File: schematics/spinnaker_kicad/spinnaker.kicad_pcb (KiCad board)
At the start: 2 copper layers, 87 x 60.3 mm, 156 parts, among them J1 L_INP, J2 R_INP, J3 L_OUT, J4 R_OUT, J5 9VDC POWER, J6 CONTROL, Q1 AO3401, U1 SpinSemi_FV-1, U10 24LC32, U11 24LC32, U12 24LC32, U13 24LC32, U14 24LC32, U15 24LC32, U16 24LC32, U17 AMS1117-3.3, U18 AMS1117-5.0, U19 MP1470, U2 TL071, U3 TL071, U4 TL071, U5 TL071, U6 PT2258, U7 MCP4728, U8 PCF8574, U9 24LC32, Y1 32768Hz

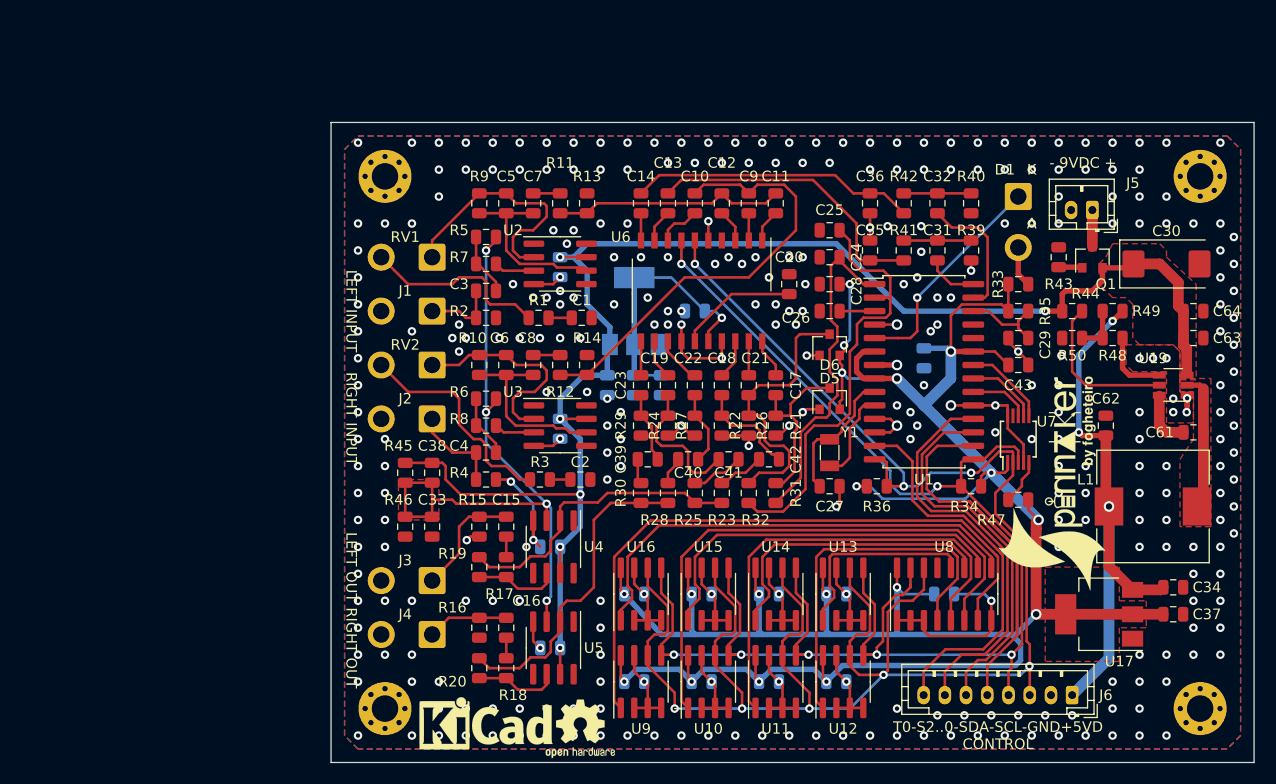
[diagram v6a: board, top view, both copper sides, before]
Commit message: Eliminación de vias sobre pads. Ligeros retoques en la PCB. Arreglamos el lío de librerías debido al cambio de versión de Kicad.
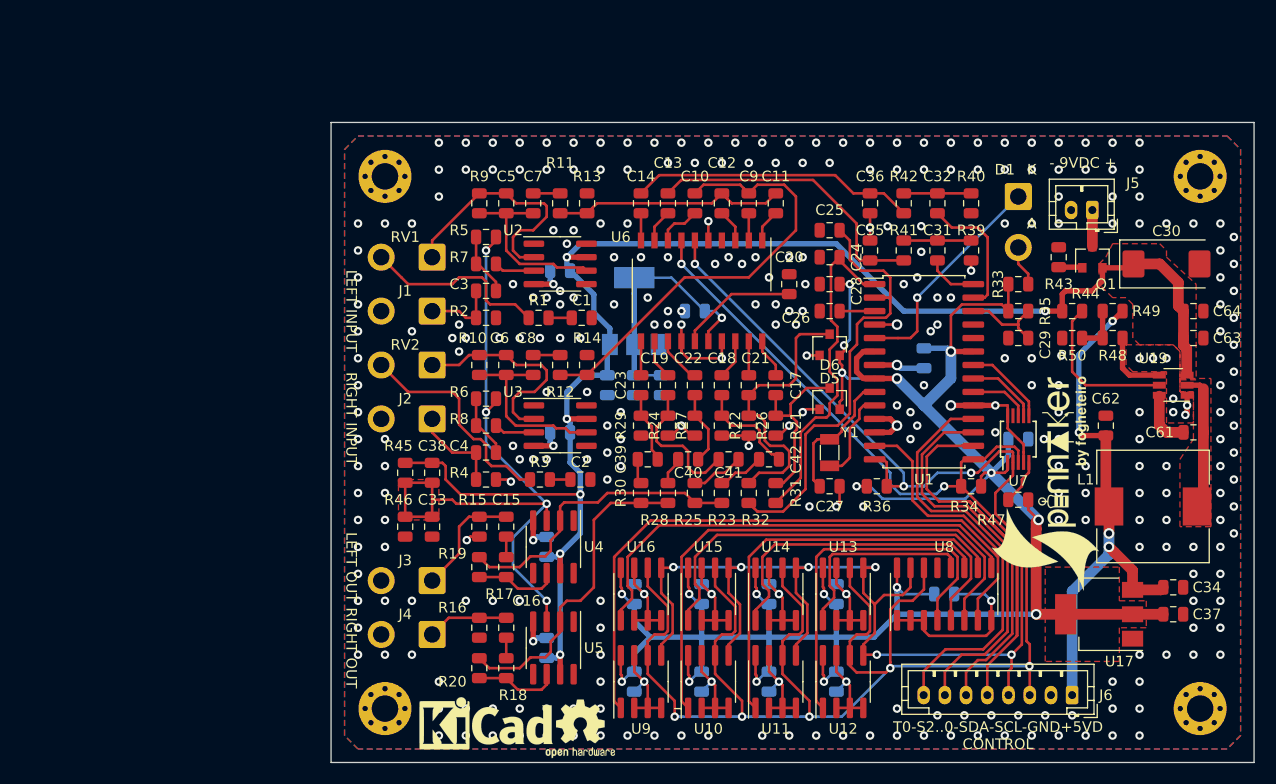
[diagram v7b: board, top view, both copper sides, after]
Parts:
- C43: moved to B.Cu
- moved C43 6.98 mm to (167.0, 87.0)
- moved G*** 3.86 mm to (158.1, 88.9)
- moved G*** 0.64 mm to (169.5, 91.2)
- moved C45 0.33 mm to (123.8, 71.1), turned to 180 degrees
- moved C47 0.33 mm to (123.8, 86.4), turned to 180 degrees
- moved C49 0.33 mm to (122.6, 97.2), turned to 90 degrees
- moved C51 0.33 mm to (122.6, 106.7), turned to 90 degrees
- turned C48 to 90 degrees
- turned C50 to 90 degrees
- turned C52 to 270 degrees
- turned C53 to 270 degrees
- turned C55 to 270 degrees
- turned C57 to 270 degrees
- turned C59 to 90 degrees
- turned C60 to 90 degrees
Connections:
- U2 pad 1: (no net) -> Net-(U2-Pad1)
- U2 pad 5: (no net) -> Net-(U2-Pad5)
- U2 pad 8: (no net) -> Net-(U2-Pad8)
- U3 pad 1: (no net) -> Net-(U3-Pad1)
- U3 pad 5: (no net) -> Net-(U3-Pad5)
- U3 pad 8: (no net) -> Net-(U3-Pad8)
- U4 pad 1: (no net) -> Net-(U4-Pad1)
- U4 pad 5: (no net) -> Net-(U4-Pad5)
- U4 pad 8: (no net) -> Net-(U4-Pad8)
- U5 pad 1: (no net) -> Net-(U5-Pad1)
- U5 pad 5: (no net) -> Net-(U5-Pad5)
- U5 pad 8: (no net) -> Net-(U5-Pad8)
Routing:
- net +3V3: track 242.4 -> 219.3 mm
- net Earth: track 155.5 -> 160.7 mm, vias 324 -> 316
- net +5VD: track 53.6 -> 49.8 mm, vias 3 -> 4
- net SDA: track 154.6 -> 151.5 mm, vias 7 -> 8
- net SCL: track 184.8 -> 187.2 mm
- net 4V5: track 65.0 -> 67.3 mm
- net Net-(S102-PadP$3): vias 0 -> 1
- net Net-(S101-PadP$3): vias 0 -> 1

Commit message: Pequeños retoques en zonas de relleno de la PCB y en la silkscreen.
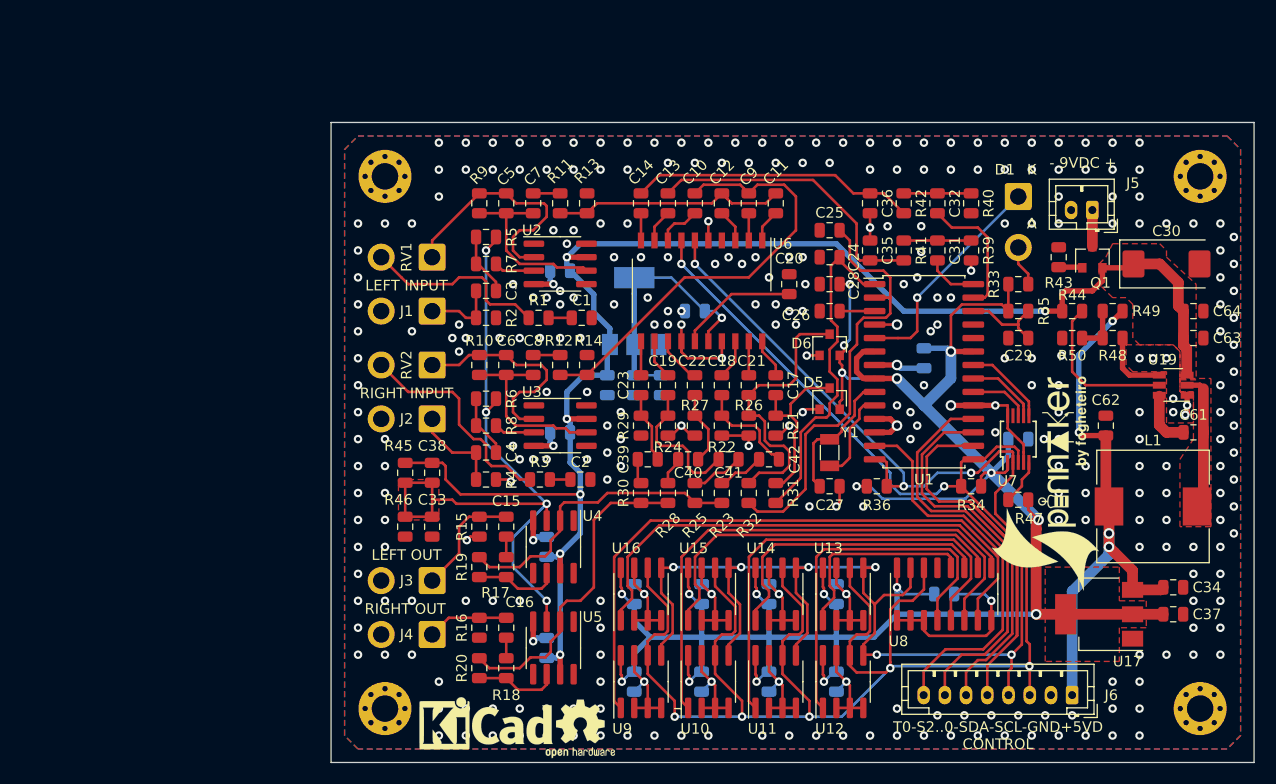
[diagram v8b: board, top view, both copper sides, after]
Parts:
- REF**: value KiCad-Logo2_12mm_SilkScreen -> KiCad-Logo2_8mm_SilkScreen; footprint Symbol:KiCad-Logo2_12mm_SilkScreen -> Symbol:KiCad-Logo2_8mm_SilkScreen
- moved REF** 42.7 mm to (123.1, 63.2)
- moved REF** 5.21 mm to (148.5, 70.1)
- moved G*** 1.65 mm to (159.6, 89.5)
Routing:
- net +5VD: track 49.8 -> 51.1 mm
- net Net-(S102-PadP$3): vias 1 -> 0
- net Earth: vias 316 -> 317
